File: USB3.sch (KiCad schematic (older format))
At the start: 42 parts, among them IC7 M24M02-DRMN6TP, IC8 TPD4E05U06QDQARQ1, J11 Conn_01x07, J12 USB3_B, U10 CYUSB3014-BZXI, U11 WE-TVS-82400102, Y3 19.2Mhz

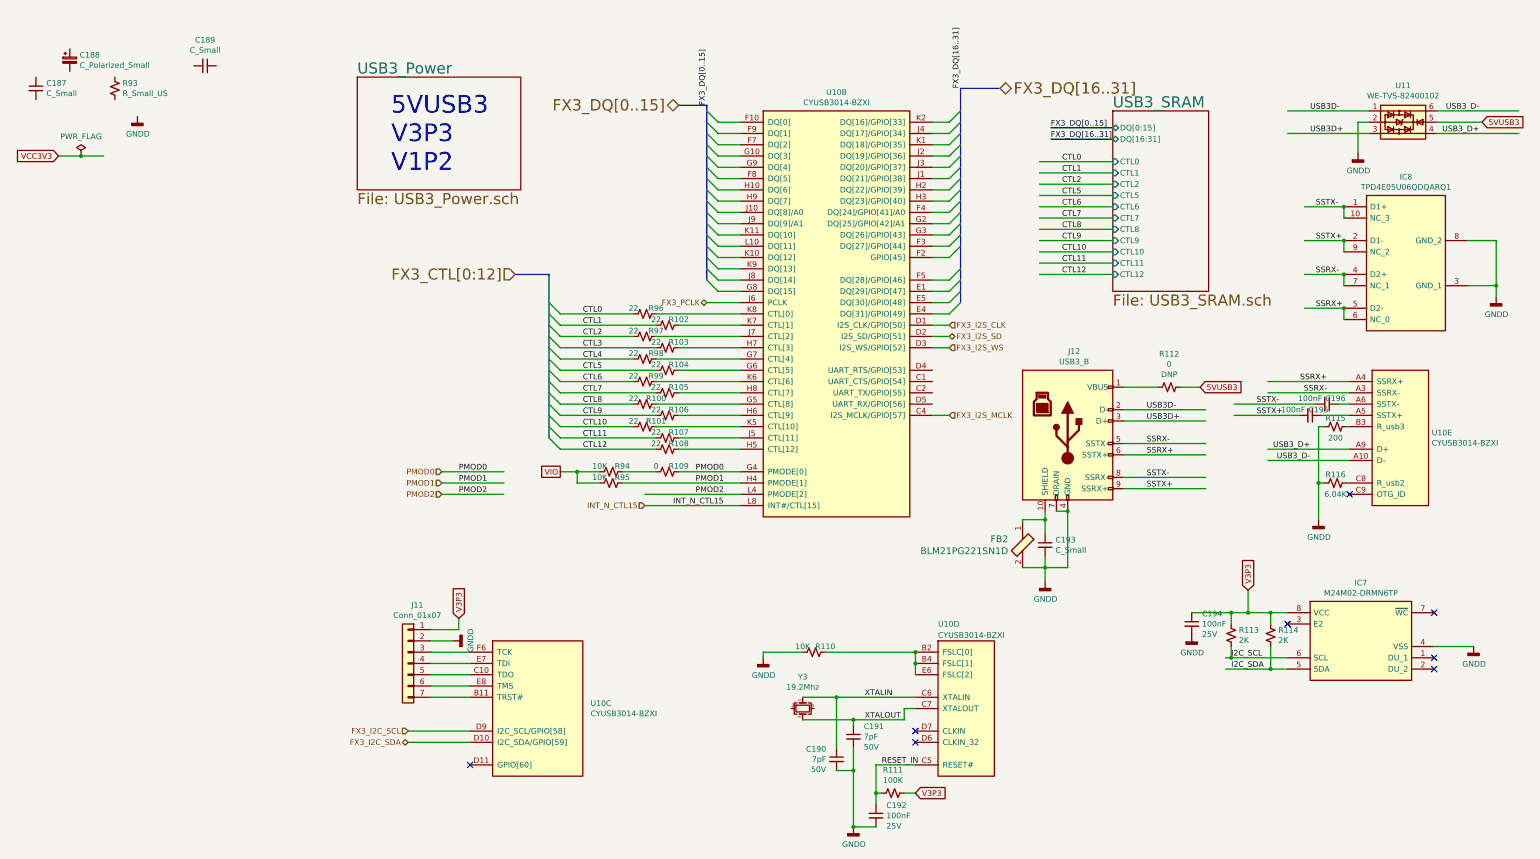
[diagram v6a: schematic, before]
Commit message: Corrected PCB import errors
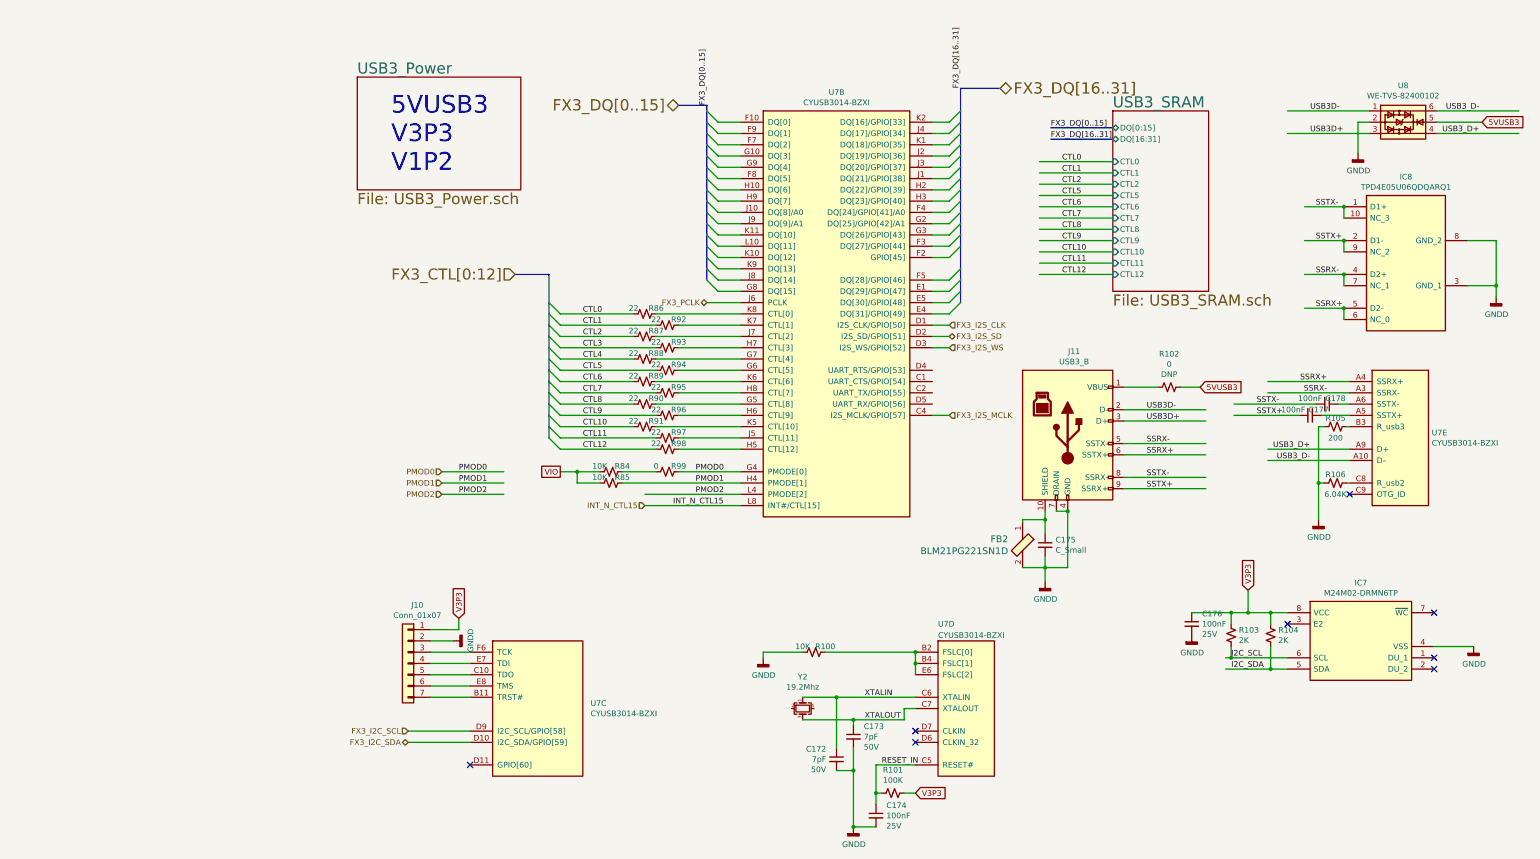
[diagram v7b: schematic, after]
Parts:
- removed C187: C_Small, Capacitor_SMD:C_0603_1608Metric_Pad1.08x0.95mm_HandSolder, symbol Device:C_Small
- removed C188: C_Polarized_Small, Capacitor_Tantalum_SMD:CP_EIA-1608-10_AVX-L_Pad1.25x1.05mm_HandSolder, symbol Device:C_Polarized_Small
- removed C189: C_Small, symbol Device:C_Small
- removed R93: R_Small_US, Resistor_SMD:R_0603_1608Metric_Pad0.98x0.95mm_HandSolder, symbol Device:R_Small_US
- IC8: footprint DQA(R-PUSON-N10) -> GM_SON:DQA_R-PUSON-N10_
- U7: renamed from U10; footprint Package_BGA:BGA121C80P11X11_1000X1000X120 -> GM_BGA:BGA121C80P11X11_1000X1000X120
- renumbered C190 to C172, C191 to C173, C192 to C174, C193 to C175, C194 to C176, C195 to C177, C196 to C178, J11 to J10, J12 to J11, R110 to R100, R111 to R101, R112 to R102, R113 to R103, R114 to R104, R115 to R105, R116 to R106, R94 to R84, R95 to R85, R96 to R86, R97 to R87, R98 to R88, R99 to R89, R100 to R90, R101 to R91, R102 to R92, R103 to R93, R104 to R94, R105 to R95, R106 to R96, R107 to R97, R108 to R98, R109 to R99, U11 to U8, Y3 to Y2
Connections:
- net labels removed: VCC3V3
- wire segments 186 -> 184
